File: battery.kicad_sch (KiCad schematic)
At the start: 32 parts, among them J3 Lipo, Q1 Q_NMOS, SW2 SW_Push, U2 BQ76920PW

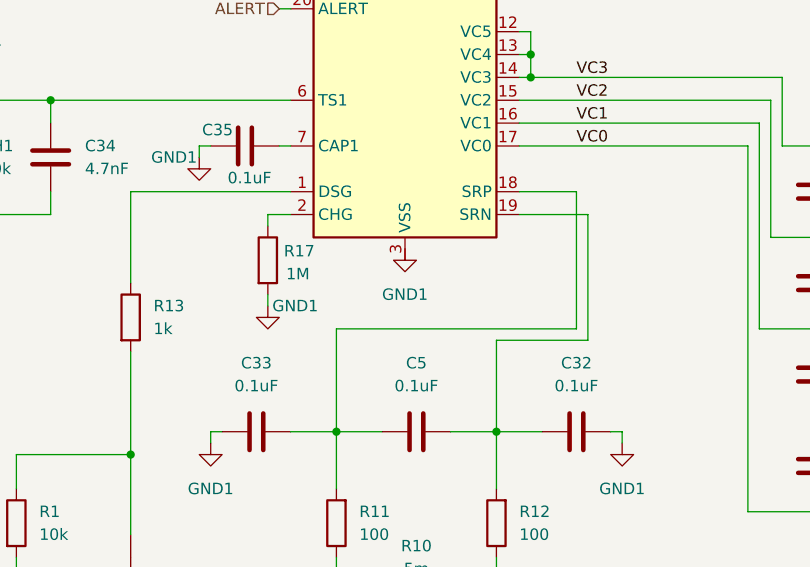
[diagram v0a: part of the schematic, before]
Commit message: fixed bad ground placement
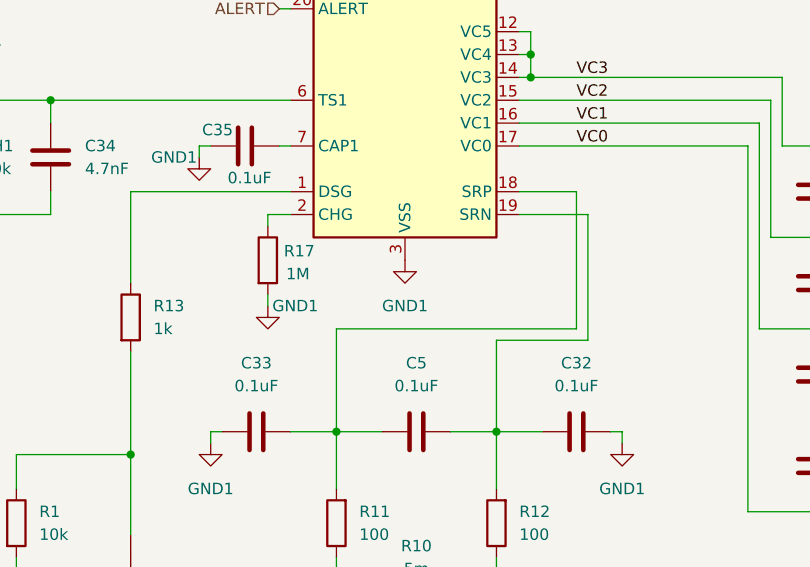
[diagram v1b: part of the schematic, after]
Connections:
- net GND1: now also U2.3 (VSS)
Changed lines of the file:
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@@
 	(symbol
 		(lib_id "power:GND1")
-		(at 166.37 104.14 0)
+		(at 166.37 105.41 0)
 		(unit 1)
 		(exclude_from_sim no)
@@
 		(fields_autoplaced yes)
 		(property "Reference" "#PWR05"
-			(at 166.37 110.49 0)
+			(at 166.37 111.76 0)
 			(effects
 				(font
@@
 		)
 		(property "Value" "GND1"
-			(at 166.37 109.22 0)
+			(at 166.37 110.49 0)
 			(effects
 				(font
@@
 		)
 		(property "Footprint" ""
-			(at 166.37 104.14 0)
+			(at 166.37 105.41 0)
 			(effects
 				(font
@@
 		)
 		(property "Datasheet" ""
-			(at 166.37 104.14 0)
+			(at 166.37 105.41 0)
 			(effects
 				(font
@@
 		)
 		(property "Description" "Power symbol creates a global label with name \"GND1\" , ground"
-			(at 166.37 104.14 0)
+			(at 166.37 105.41 0)
 			(effects
 				(font

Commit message: fixed whatever was going on with i2c
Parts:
- BT1: footprint Connector_AMASS:AMASS_XT60-F_1x02_P7.20mm_Vertical -> Connector_AMASS:AMASS_XT60-M_1x02_P7.20mm_Vertical
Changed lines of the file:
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@@
 			)
 		)
-		(property "Footprint" "Connector_AMASS:AMASS_XT60-F_1x02_P7.20mm_Vertical"
+		(property "Footprint" "Connector_AMASS:AMASS_XT60-M_1x02_P7.20mm_Vertical"
 			(at 90.17 106.426 90)
 			(effects

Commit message: added footprints for almost everything
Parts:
- R1, R13: footprint (none) -> Resistor_SMD:R_0402_1005Metric
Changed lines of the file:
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@@
 			)
 		)
-		(property "Footprint" ""
+		(property "Footprint" "Resistor_SMD:R_0402_1005Metric"
 			(at 121.412 134.62 90)
 			(effects
@@
 			)
 		)
-		(property "Footprint" ""
+		(property "Footprint" "Resistor_SMD:R_0402_1005Metric"
 			(at 134.112 111.76 90)
 			(effects

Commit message: added schematics and footprints to project
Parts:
- J3: symbol International_Symbols:Lipo_Pinout -> Dry_Lettuce:Lipo_Pinout
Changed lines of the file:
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@@
 	)
 	(symbol
-		(lib_id "International_Symbols:Lipo_Pinout")
+		(lib_id "Dry_Lettuce:Lipo_Pinout")
 		(at 251.46 88.9 0)
 		(unit 1)

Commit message: working on bms layout v2
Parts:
- removed Q1: Q_NMOS, Package_TO_SOT_THT:TO-247-3_Horizontal_TabDown, symbol Device:Q_NMOS
- added Q2: Q_NMOS_GDS, Package_TO_SOT_THT:TO-247-3_Horizontal_TabDown, symbol Transistor_FET:Q_NMOS_GDS
- SW2: footprint Button_Switch_SMD:SW_Push_1P1T_NO_CK_PTS125Sx43PSMTR -> Button_Switch_SMD:SW_Push_1P1T_NO_CK_KSC6xxJ
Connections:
- net TS1_SW: now reaches R14.1, SW2.2
- net TS1: now reaches C34.1, R14.2, TH1.1, U2.6 (TS1)
- net SRN: now reaches C32.1, C5.2, R12.2, U2.19 (SRN)
- net SRP: now reaches C33.2, C5.1, R11.2, U2.18 (SRP)
- net REGSRC: now reaches C37.1, R15.2, U2.9 (REGSRC)
- net DSG: now reaches R13.1, U2.1 (DSG)
- net BAT: now reaches C38.1, R16.2, U2.10 (BAT)
- net CHG: now reaches R17.1, U2.2 (CHG)
- net CAP1: now reaches C35.2, U2.7 (CAP1)
- net DSG_DRAIN: now reaches R10.1, R11.1
- net DSG_DRAIN: now also Q2.2 (D)
- net DSG_GATE: now reaches R1.1, R13.2
- net DSG_GATE: now also Q2.1 (G)
- net DSG_SOURCE: now reaches F1.2, R1.2
- net DSG_SOURCE: now also Q2.3 (S)
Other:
- moved on the sheet: C35, R17

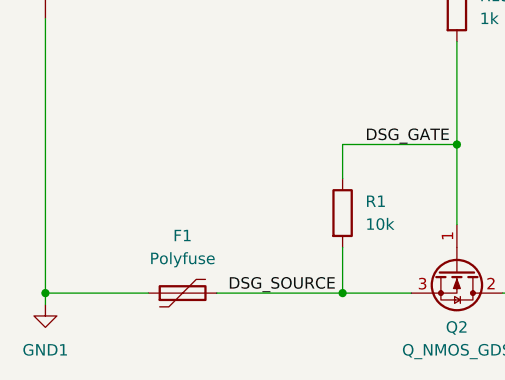
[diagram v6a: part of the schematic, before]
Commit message: added some tracks
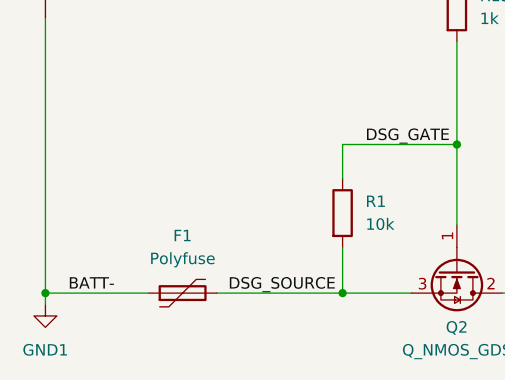
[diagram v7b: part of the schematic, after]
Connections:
- net BATT- is gone; now on net GND1: R10.2, R12.1
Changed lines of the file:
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@@
+		)
+	)
+	(label "BATT-"
+		(at 92.71 143.51 0)
+		(effects
+			(font
+				(size 1.27 1.27)
+			)
+			(justify left bottom)
 		)
 	)

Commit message: idrk what i changed tbh but probably not anything important
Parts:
- J3: footprint Connector_JST:JST_XH_B4B-XH-AM_1x04_P2.50mm_Vertical -> Connector_JST:JST_XH_B4B-XH-A_1x04_P2.50mm_Vertical
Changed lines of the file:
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@@
 			)
 		)
-		(property "Footprint" "Connector_JST:JST_XH_B4B-XH-AM_1x04_P2.50mm_Vertical"
+		(property "Footprint" "Connector_JST:JST_XH_B4B-XH-A_1x04_P2.50mm_Vertical"
 			(at 251.46 88.9 0)
 			(effects
